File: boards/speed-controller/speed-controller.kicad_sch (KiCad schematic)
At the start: 36 parts, among them J1 Screw_Terminal_01x02, J2 Screw_Terminal_01x02, J3 Screw_Terminal_01x02, J4 USB_B_Micro, Q1 BSS138, Q2 BSS138, SW1 SW_Push, U3 L298HN, U4 ESP32-WROOM-32D, U5 MCP2200-I-MQ

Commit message: Added annotations
Signed-off-by: Computroniks <mnickson@sidingsmedia.com>
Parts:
- gave numbers to parts that had none: 2
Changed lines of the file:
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@@
   (symbol (lib_id "Regulator_Linear:LM317_SOT-223") (at 93.98 91.44 0) (unit 1)
     (in_bom yes) (on_board yes) (fields_autoplaced)
-    (property "Reference" "U?" (id 0) (at 93.98 85.5685 0))
+    (property "Reference" "U2" (id 0) (at 93.98 85.5685 0))
     (property "Value" "LM317_SOT-223" (id 1) (at 93.98 88.3436 0))
     (property "Footprint" "Package_TO_SOT_SMD:SOT-223-3_TabPin2" (id 2) (at 93.98 85.09 0)
@@
   (symbol (lib_id "Regulator_Linear:LM317_SOT-223") (at 39.37 90.17 0) (unit 1)
     (in_bom yes) (on_board yes) (fields_autoplaced)
-    (property "Reference" "U?" (id 0) (at 39.37 84.2985 0))
+    (property "Reference" "U1" (id 0) (at 39.37 84.2985 0))
     (property "Value" "LM317_SOT-223" (id 1) (at 39.37 87.0736 0))
     (property "Footprint" "Package_TO_SOT_SMD:SOT-223-3_TabPin2" (id 2) (at 39.37 83.82 0)
@@
       (reference "SW1") (unit 1) (value "SW_Push") (footprint "Button_Switch_SMD:SW_Push_1P1T_NO_6x6mm_H9.5mm")
     )
+    (path "/e03bb906-5c6e-470d-a0a5-2488e1793551"
+      (reference "U1") (unit 1) (value "LM317_SOT-223") (footprint "Package_TO_SOT_SMD:SOT-223-3_TabPin2")
+    )
+    (path "/7f0cc443-d897-4e16-abe0-1a89611d04cf"
+      (reference "U2") (unit 1) (value "LM317_SOT-223") (footprint "Package_TO_SOT_SMD:SOT-223-3_TabPin2")
+    )
     (path "/00000000-0000-0000-0000-000061d063aa"
       (reference "U3") (unit 1) (value "L298HN") (footprint "Package_TO_SOT_THT:TO-220-15_P2.54x2.54mm_StaggerOdd_Lead4.58mm_Vertical")
@@
       (reference "U5") (unit 1) (value "MCP2200-I-MQ") (footprint "Package_DFN_QFN:QFN-20-1EP_5x5mm_P0.65mm_EP3.35x3.35mm")
     )
-    (path "/7f0cc443-d897-4e16-abe0-1a89611d04cf"
-      (reference "U?") (unit 1) (value "LM317_SOT-223") (footprint "Package_TO_SOT_SMD:SOT-223-3_TabPin2")
-    )
-    (path "/e03bb906-5c6e-470d-a0a5-2488e1793551"
-      (reference "U?") (unit 1) (value "LM317_SOT-223") (footprint "Package_TO_SOT_SMD:SOT-223-3_TabPin2")
-    )
-  )
+  )

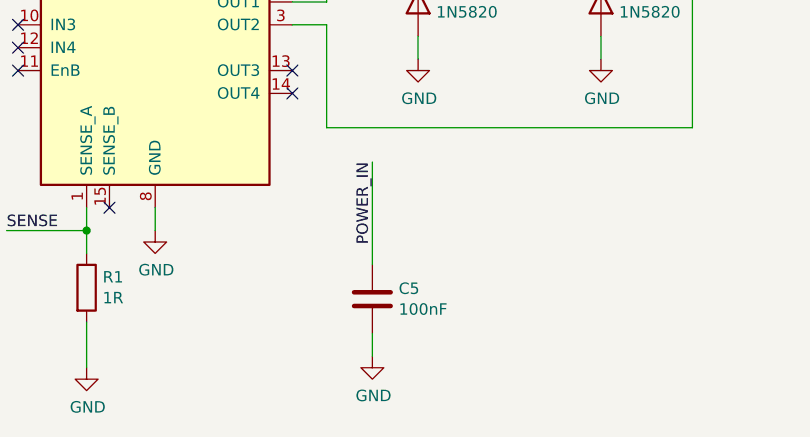
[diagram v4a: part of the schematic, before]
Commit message: Removed unnecessary components
Signed-off-by: Computroniks <mnickson@sidingsmedia.com>
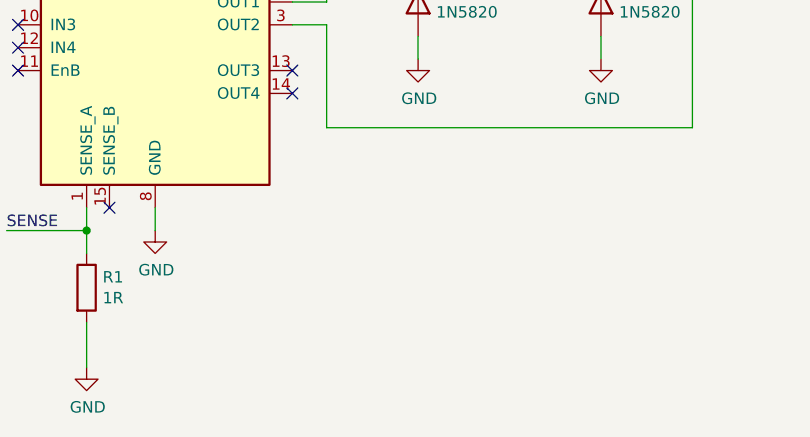
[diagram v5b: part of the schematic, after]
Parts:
- removed C5: 100nF, Capacitor_SMD:C_0805_2012Metric, symbol Device:C
- C6: footprint Capacitor_SMD:C_0805_2012Metric -> Capacitor_SMD:CP_Elec_4x3
- D1, D2, D3, D4: footprint Diode_SMD:D_0805_2012Metric -> Diode_SMD:D_SMC
- R1: footprint Resistor_SMD:R_0805_2012Metric -> Resistor_THT:R_Axial_Power_L20.0mm_W6.4mm_P22.40mm
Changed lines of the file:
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@@
-    (stroke (width 0) (type default) (color 0 0 0 0))
-  )
-  (wire (pts (xy 67.31 163.83) (xy 67.31 175.26))
     (stroke (width 0) (type default) (color 0 0 0 0))
   )
@@
     (stroke (width 0) (type default) (color 0 0 0 0))
   )
-  (wire (pts (xy 67.31 185.42) (xy 67.31 182.88))
-    (stroke (width 0) (type default) (color 0 0 0 0))
-  )
   (wire (pts (xy 114.3 91.44) (xy 121.92 91.44))
     (stroke (width 0) (type default) (color 0 0 0 0))
@@
   )
   (text "Line" (at 21.59 46.99 180)
-    (effects (font (size 1.27 1.27)) (justify right bottom))
-  )
-  (label "POWER_IN" (at 67.31 163.83 270)
     (effects (font (size 1.27 1.27)) (justify right bottom))
   )
@@
       (effects (font (size 1.27 1.27)) (justify left))
     )
-    (property "Footprint" "Resistor_SMD:R_0805_2012Metric" (id 2) (at 33.782 177.8 90)
+    (property "Footprint" "Resistor_THT:R_Axial_Power_L20.0mm_W6.4mm_P22.40mm" (id 2) (at 33.782 177.8 90)
       (effects (font (size 1.27 1.27)) hide)
     )
@@
       (effects (font (size 1.27 1.27)) (justify left))
     )
-    (property "Footprint" "Diode_SMD:D_0805_2012Metric" (id 2) (at 67.945 146.05 0)
+    (property "Footprint" "Diode_SMD:D_SMC" (id 2) (at 67.945 146.05 0)
       (effects (font (size 1.27 1.27)) hide)
     )
@@
       (effects (font (size 1.27 1.27)) (justify left))
     )
-    (property "Footprint" "Diode_SMD:D_0805_2012Metric" (id 2) (at 67.945 135.89 0)
+    (property "Footprint" "Diode_SMD:D_SMC" (id 2) (at 67.945 135.89 0)
       (effects (font (size 1.27 1.27)) hide)
     )
@@
       (effects (font (size 1.27 1.27)) (justify left))
     )
-    (property "Footprint" "Diode_SMD:D_0805_2012Metric" (id 2) (at 88.265 135.89 0)
+    (property "Footprint" "Diode_SMD:D_SMC" (id 2) (at 88.265 135.89 0)
       (effects (font (size 1.27 1.27)) hide)
     )
@@
       (effects (font (size 1.27 1.27)) (justify left))
     )
-    (property "Footprint" "Diode_SMD:D_0805_2012Metric" (id 2) (at 88.265 146.05 0)
+    (property "Footprint" "Diode_SMD:D_SMC" (id 2) (at 88.265 146.05 0)
       (effects (font (size 1.27 1.27)) hide)
     )
@@
     (pin "1")
   )
-  (symbol (lib_id "Device:C") (at 67.31 179.07 0) (unit 1)
-    (in_bom yes) (on_board yes)
-    (property "Reference" "C5" (id 0) (at 70.231 177.9016 0)
-      (effects (font (size 1.27 1.27)) (justify left))
-    )
-    (property "Value" "100nF" (id 1) (at 70.231 180.213 0)
-      (effects (font (size 1.27 1.27)) (justify left))
-    )
-    (property "Footprint" "Capacitor_SMD:C_0805_2012Metric" (id 2) (at 68.2752 182.88 0)
-      (effects (font (size 1.27 1.27)) hide)
-    )
-    (property "Datasheet" "~" (id 3) (at 67.31 179.07 0)
-      (effects (font (size 1.27 1.27)) hide)
-    )
-    (pin "1")
-    (pin "2")
-  )
-  (symbol (lib_id "power:GND") (at 67.31 185.42 0) (unit 1)
-    (in_bom yes) (on_board yes)
-    (property "Reference" "#PWR010" (id 0) (at 67.31 191.77 0)
-      (effects (font (size 1.27 1.27)) hide)
-    )
-    (property "Value" "GND" (id 1) (at 67.437 189.8142 0))
-    (property "Footprint" "" (id 2) (at 67.31 185.42 0)
-      (effects (font (size 1.27 1.27)) hide)
-    )
-    (property "Datasheet" "" (id 3) (at 67.31 185.42 0)
-      (effects (font (size 1.27 1.27)) hide)
-    )
-    (pin "1")
-  )
   (symbol (lib_id "power:+5V") (at 40.64 130.81 0) (unit 1)
     (in_bom yes) (on_board yes)
@@
       (effects (font (size 1.27 1.27)) (justify left))
     )
-    (property "Footprint" "Capacitor_SMD:C_0805_2012Metric" (id 2) (at 108.9152 43.18 0)
+    (property "Footprint" "Capacitor_SMD:CP_Elec_4x3" (id 2) (at 108.9152 43.18 0)
       (effects (font (size 1.27 1.27)) hide)
     )
@@
       (reference "#PWR09") (unit 1) (value "+3V3") (footprint "")
     )
-    (path "/00000000-0000-0000-0000-000061d7d120"
-      (reference "#PWR010") (unit 1) (value "GND") (footprint "")
-    )
     (path "/00000000-0000-0000-0000-000061d529bf"
       (reference "#PWR011") (unit 1) (value "GND") (footprint "")
@@
       (reference "C4") (unit 1) (value "1uF") (footprint "Capacitor_SMD:CP_Elec_4x3")
     )
-    (path "/00000000-0000-0000-0000-000061d7c786"
-      (reference "C5") (unit 1) (value "100nF") (footprint "Capacitor_SMD:C_0805_2012Metric")
-    )
     (path "/00000000-0000-0000-0000-000061d8b602"
-      (reference "C6") (unit 1) (value "1uF") (footprint "Capacitor_SMD:C_0805_2012Metric")
+      (reference "C6") (unit 1) (value "1uF") (footprint "Capacitor_SMD:CP_Elec_4x3")
     )
     (path "/00000000-0000-0000-0000-000061d4b03a"
-      (reference "D1") (unit 1) (value "1N5820") (footprint "Diode_SMD:D_0805_2012Metric")
+      (reference "D1") (unit 1) (value "1N5820") (footprint "Diode_SMD:D_SMC")
     )
     (path "/00000000-0000-0000-0000-000061d42326"
-      (reference "D2") (unit 1) (value "1N5820") (footprint "Diode_SMD:D_0805_2012Metric")
+      (reference "D2") (unit 1) (value "1N5820") (footprint "Diode_SMD:D_SMC")
     )
     (path "/00000000-0000-0000-0000-000061d54f6a"
-      (reference "D3") (unit 1) (value "1N5820") (footprint "Diode_SMD:D_0805_2012Metric")
+      (reference "D3") (unit 1) (value "1N5820") (footprint "Diode_SMD:D_SMC")
     )
     (path "/00000000-0000-0000-0000-000061d54f74"
-      (reference "D4") (unit 1) (value "1N5820") (footprint "Diode_SMD:D_0805_2012Metric")
+      (reference "D4") (unit 1) (value "1N5820") (footprint "Diode_SMD:D_SMC")
     )
     (path "/5579b8b9-0e39-41bb-8f77-3ead56330726"
@@
     )
     (path "/00000000-0000-0000-0000-000061d06cae"
-      (reference "R1") (unit 1) (value "1R") (footprint "Resistor_SMD:R_0805_2012Metric")
+      (reference "R1") (unit 1) (value "1R") (footprint "Resistor_THT:R_Axial_Power_L20.0mm_W6.4mm_P22.40mm")
     )
     (path "/00000000-0000-0000-0000-000061d1ba28"
